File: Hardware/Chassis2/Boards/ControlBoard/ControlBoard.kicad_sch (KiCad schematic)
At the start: 16 parts, among them J1 Conn_02x08_Counter_Clockwise, J10 Conn_02x03_Counter_Clockwise, J11 TBP01R2W-508-06BE, J12 Conn_02x08_Counter_Clockwise, J13 Conn_02x03_Counter_Clockwise, J14 Conn_01x10, J2 Conn_01x02, J7 Conn_02x08_Counter_Clockwise

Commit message: update hw revision 7
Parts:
- removed J1: Conn_02x08_Counter_Clockwise, Connector_PinHeader_2.54mm:PinHeader_2x08_P2.54mm_Vertical, symbol Connector_Generic:Conn_02x08_Counter_Clockwise
- removed J14: Conn_01x10, Connector_PinHeader_2.54mm:PinHeader_1x10_P2.54mm_Vertical, symbol Connector_Generic:Conn_01x10
- removed J2: Conn_01x02, Connector_PinHeader_2.54mm:PinHeader_1x02_P2.54mm_Vertical, symbol Connector_Generic:Conn_01x02
- added J14: Conn_02x08_Counter_Clockwise, Connector_PinHeader_2.54mm:PinHeader_2x08_P2.54mm_Vertical, symbol Connector_Generic:Conn_02x08_Counter_Clockwise
- added J2: Conn_02x10_Counter_Clockwise, symbol Connector_Generic:Conn_02x10_Counter_Clockwise
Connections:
- net +12V_A: now also J2.20 (Pin_20)
- net +3.3V_A: now also J14.10 (Pin_10), J2.18 (Pin_18)
- net DRIVER_RESET: now also J2.4 (Pin_4)
- net FAULT: now also J2.2 (Pin_2)
- net GND_A: now also J14.1 (Pin_1), J14.15 (Pin_15), J14.7 (Pin_7), J2.1 (Pin_1), J2.12 (Pin_12), J2.14 (Pin_14), J2.17 (Pin_17), J2.9 (Pin_9)
- net PH_U_H: now also J2.6 (Pin_6)
- net PH_U_L: now also J2.5 (Pin_5)
- net PH_V_H: now also J2.8 (Pin_8)
- net PH_V_L: now also J2.7 (Pin_7)
- net PH_W_H: now also J2.16 (Pin_16)
- net PH_W_L: now also J2.15 (Pin_15)
- net READY: now also J2.3 (Pin_3)
- net VSENSE_DC_LINK_Y renamed VS_DC_LINK_Y
- net VSENSE_GND_Y renamed VS_GND_Y
- net VSENSE_PH_U_Y renamed VS_PH_U_Y
- net VSENSE_PH_V_Y renamed VS_PH_V_Y
- net VSENSE_PH_W_Y renamed VS_PH_W_Y
- new net +12V_IN_A: J14.16 (Pin_16)
- new net CP_BOOTSEL: J14.14 (Pin_14)
- new net CP_RESET: J14.11 (Pin_11)
- new net CP_SWCLK: J14.13 (Pin_13)
- new net CP_SWDIO: J14.12 (Pin_12)
- new net GATE_DRIVE_PWR1_ENABLE: J2.19 (Pin_19)
- new net GATE_DRIVE_PWR1_FB: J2.10 (Pin_10)
- new net GATE_DRIVE_PWR2_ENABLE: J2.13 (Pin_13)
- new net GATE_DRIVE_PWR2_FB: J2.11 (Pin_11)
- new net MP_BOOTSEL: J14.3 (Pin_3)
- new net MP_RESET: J14.6 (Pin_6)
- new net MP_SWCLK: J14.4 (Pin_4)
- new net MP_SWDIO: J14.5 (Pin_5)
- new net MP_SWO: J14.2 (Pin_2)
- new net USB_DM: J14.9 (Pin_9)
- new net USB_DP: J14.8 (Pin_8)
- no-connect marks 4 -> 2
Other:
- removed sheet USB Interface
- sheet ADC ports: added SPI_MISO_A, SPI_MOSI_A; removed SPI_RX_A, SPI_TX_A
- sheet CAN Transciever ports: added A_CAN_RX, A_CAN_TX, B_CAN_RX, B_CAN_TX; removed CAN_RX, CAN_TX
- sheet CAN Transciever1 ports: added A_CAN_RX, A_CAN_TX, B_CAN_RX, B_CAN_TX; removed CAN_RX, CAN_TX
- sheet Control ports: added CP_BOOT_SEL, CP_DEBUG_JTCK_SWCLK, CP_DEBUG_JTMS_SWDIO, CP_FDCAN2_RX, CP_FDCAN2_TX, CP_FDCAN3_RX, CP_FDCAN3_TX, CP_GATE_DRIVE_PWR2_ENABLE, CP_RESET, CP_USB_DM, CP_USB_DP, MP_BOOT_SEL, MP_CANBUS_12V_POWER_ENABLE, MP_DEBUG_JTCK_SWCLK, MP_DEBUG_JTCK_SWDIO, MP_DEBUG_NJTRST, MP_DEBUG_SWO, MP_DEBUG_TRGIO, MP_FDCAN1_RX, MP_FDCAN1_TX, MP_FDCAN2_RX, MP_FDCAN2_TX, MP_GATE_DRIVE_PWR1_ENABLE, MP_PERIPHERAL_POWER_ENABLE, MP_RESET, MP_SPI2_CS, MP_SPI2_MISO, MP_SPI2_MOSI, MP_SPI2_SCK, MP_TEMP_SENSE_2, MP_TEMP_SENSE_3, MP_USER_DIN_5, MP_USER_DIN_6, MP_USER_DIN_7, MP_USER_DIN_8, MP_USER_DOUT_1, MP_USER_DOUT_2, MP_USER_DOUT_3, MP_USER_DOUT_4, MP_VSENSE_ISO_ADC_INTERRUPT, SN_CUR_SENSE_DC_LINK_REF, SN_CUR_SENSE_DC_LINK_SIG, SN_CUR_SENSE_PH_U_REF, SN_CUR_SENSE_PH_U_SIG, SN_CUR_SENSE_PH_V_REF, SN_CUR_SENSE_PH_V_SIG, SN_CUR_SENSE_PH_W_REF, SN_CUR_SENSE_PH_W_SIG, SN_GATE_DRIVE_FAULT, SN_GATE_DRIVE_PWR1_FB, SN_GATE_DRIVE_PWR2_FB, SN_GATE_DRIVE_READY, SN_GATE_DRIVE_RESET, SN_HALL_U_ENCODER_SIN, SN_HALL_V_ENCODER_COS, SN_HALL_W, SN_MOTOR_TEMP, SN_PH_U_HIGH, SN_PH_U_LOW, SN_PH_V_HIGH, SN_PH_V_LOW, SN_PH_W_HIGH, SN_PH_W_LOW, SN_TEMP_SENSE_1, SN_THROTTLE_A, SN_THROTTLE_B, SN_USER_DIN_1, SN_USER_DIN_2, SN_USER_DIN_3, SN_USER_DIN_4; removed BOOT_SEL, CANBUS_12V_POWER_ENABLE, DC_LINK_CURRENT_SENSE, DC_LINK_CURRENT_SENSE_REF, DEBUG_JTCK-SWCLK, DEBUG_JTCK-SWDIO, DEBUG_NJTRST, DEBUG_SWO, DEBUG_TRGIO, FDCAN1_RX, FDCAN1_TX, FDCAN2_RX, FDCAN2_TX, GATE_DRIVER_FAULT, GATE_DRIVER_POWER_ENABLE, GATE_DRIVER_READY, GATE_DRIVER_RESET, HALL_U_ENCODER_SIN, HALL_V_ENCODER_COS, HALL_W, MOTOR_TEMP, NRST, PERIPHERAL_POWER_ENABLE, PHASE_U_CURRENT_SENSE, PHASE_U_CURRENT_SENSE_REF, PHASE_U_HIGH, PHASE_U_LOW, PHASE_V_CURRENT_SENSE, PHASE_V_CURRENT_SENSE_REF, PHASE_V_HIGH, PHASE_V_LOW, PHASE_W_CURRENT_SENSE, PHASE_W_CURRENT_SENSE_REF, PHASE_W_HIGH, PHASE_W_LOW, SPI1_CS, SPI2_MISO, SPI2_MOSI, SPI2_SCK, TEMP_SENSE_1, TEMP_SENSE_2, TEMP_SENSE_3, THROTTLE_A, THROTTLE_B, USART3_RX, USART3_TX, USER_DIN_1, USER_DIN_2, USER_DIN_3, USER_DIN_4, USER_DIN_5, USER_DIN_6, USER_DIN_7, USER_DIN_8, USER_DOUT_1, USER_DOUT_2, USER_DOUT_3, USER_DOUT_4, VSENSE_ISO_ADC_INTERRUPT
- note added: "Connector from gate drivers Includes multiple redundant SSO (six-switch-off) pathways: - via gate drive reset - via gate drive power enable 1 - via gate drive power enable 2 (Gate driver power enable implemnts 1oo2, with monitoring feedback)."
- note added: "Connector to IO board Digital Outputs provided here to IOBoard."
- note added: "Connector to IO board Provides dual fully isolated canbus interfaces (isolated from each-other as well) 60v tolerant"
- note added: "Control system has dual independent mcus, targeting ASIL decomposition. Independently monitored switching commands, current responses, canbus commands + faults Please see HARA under documentation for additional informaton."
- note added: "SINGLE WIRE DEBUG / PROGRAMMING USB INTERFACE TO TOP IO BOARD +12V TO CTRL BOARD FROM IO BOARD"
- note added: "This design has been implemented to provide multiple redundant pathways to SSO (Six-switch off) / STO (Safe torque-off). SSO/STO is the default safe-state of the inverter please (see Hazard And Risk Assessment documentation) Additionally, while best effort has been made to implement functional safety best practices, please note that no formal independent review has taken place, and therefore no f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"
- note added: "feedback pins are 0-3.3v binary (3.3v expected when +12v present)"
- note added: "onboard power regulator section, for 3.3v mcu power, +5v current sense, etc"
- note added: "voltage sense connector ISOLATED, HIGH VOLTAGE!"
- note removed: "Connector from gate drivers"
- note removed: "SINGLE WIRE DEBUG / PROGRAMMING"
- company: (none) -> Corzine Lab, University of California, Santa Cruz
- title: (none) -> Open Inverter Platform - Control Board
- moved on the sheet: H1, H2, H3, H4, H5, H6, H7, H8, J10, J13, J7

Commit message: Update boards
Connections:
- net GATE_DRIVE_PWR1_FB: no longer J2.10 (Pin_10)
- net GATE_DRIVE_PWR2_FB: no longer J2.11 (Pin_11)
- new net GATE_DRIVE_PWR1_FEEDBACK: J2.10 (Pin_10)
- new net GATE_DRIVE_PWR2_FEEDBACK: J2.11 (Pin_11)
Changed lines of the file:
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@@
-		)
-	)
-	(label "GATE_DRIVE_PWR2_FB"
-		(at 64.77 44.45 0)
-		(effects
-			(font
-				(size 1.27 1.27)
-			)
-			(justify left bottom)
 		)
 	)
@@
 			)
 			(justify left bottom)
-		)
-	)
-	(label "GATE_DRIVE_PWR1_FB"
-		(at 52.07 44.45 180)
-		(effects
-			(font
-				(size 1.27 1.27)
-			)
-			(justify right bottom)
 		)
 	)
@@
 		)
 	)
+	(hierarchical_label "GATE_DRIVE_PWR1_FEEDBACK"
+		(shape input)
+		(at 52.07 44.45 180)
+		(effects
+			(font
+				(size 1.27 1.27)
+			)
+			(justify right)
+		)
+	)
 	(hierarchical_label "GND_A"
 		(shape input)
@@
 		(effects
 			(font
+				(size 1.27 1.27)
+			)
+			(justify left)
+		)
+	)
+	(hierarchical_label "GATE_DRIVE_PWR2_FEEDBACK"
+		(shape input)
+		(at 64.77 44.45 0)
+		(effects
+			(font

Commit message: eod 2026-07-08
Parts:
- J11: footprint SHDR6W100P0X508_1X6_4064X850X1240P -> InverterCom:SHDR6W100P0X508_1X6_4064X850X1240P
- J2: footprint (none) -> Connector_PinSocket_2.54mm:PinSocket_2x10_P2.54mm_Vertical
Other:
- sheet TemperatureSensors ports: added MOTOR_TEMP_IN, MOTOR_TEMP_V; removed none

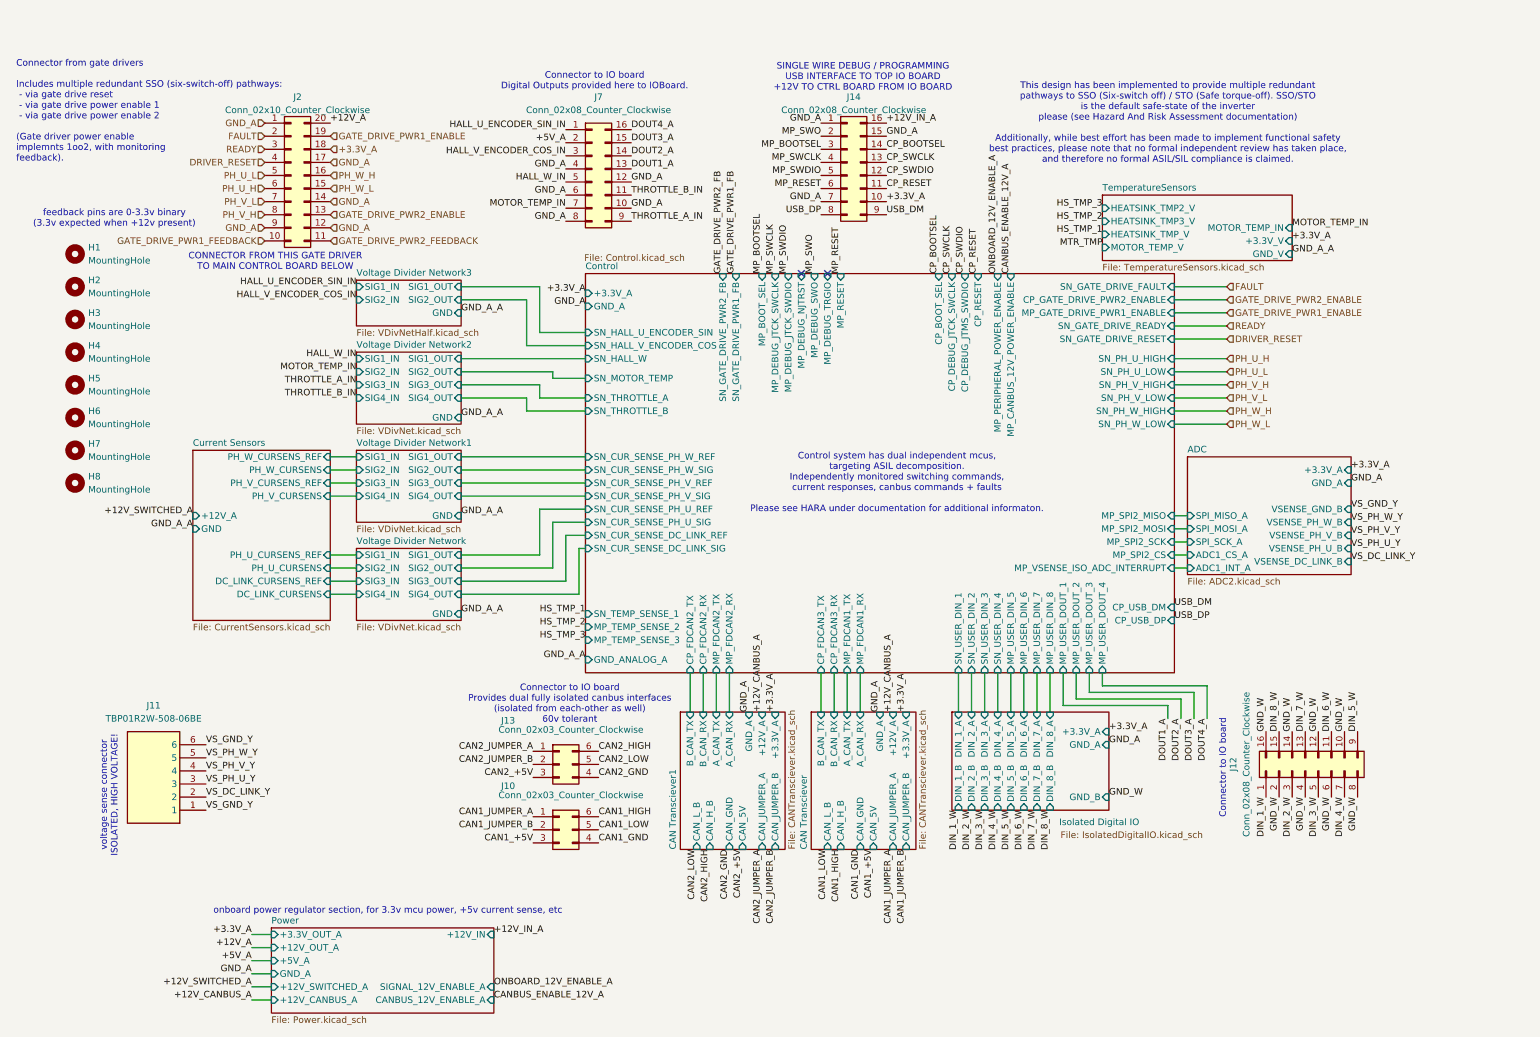
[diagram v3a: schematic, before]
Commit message: Add Schematic / Controlboard Support for Multi-Drive Mulit-Phase, DDCP
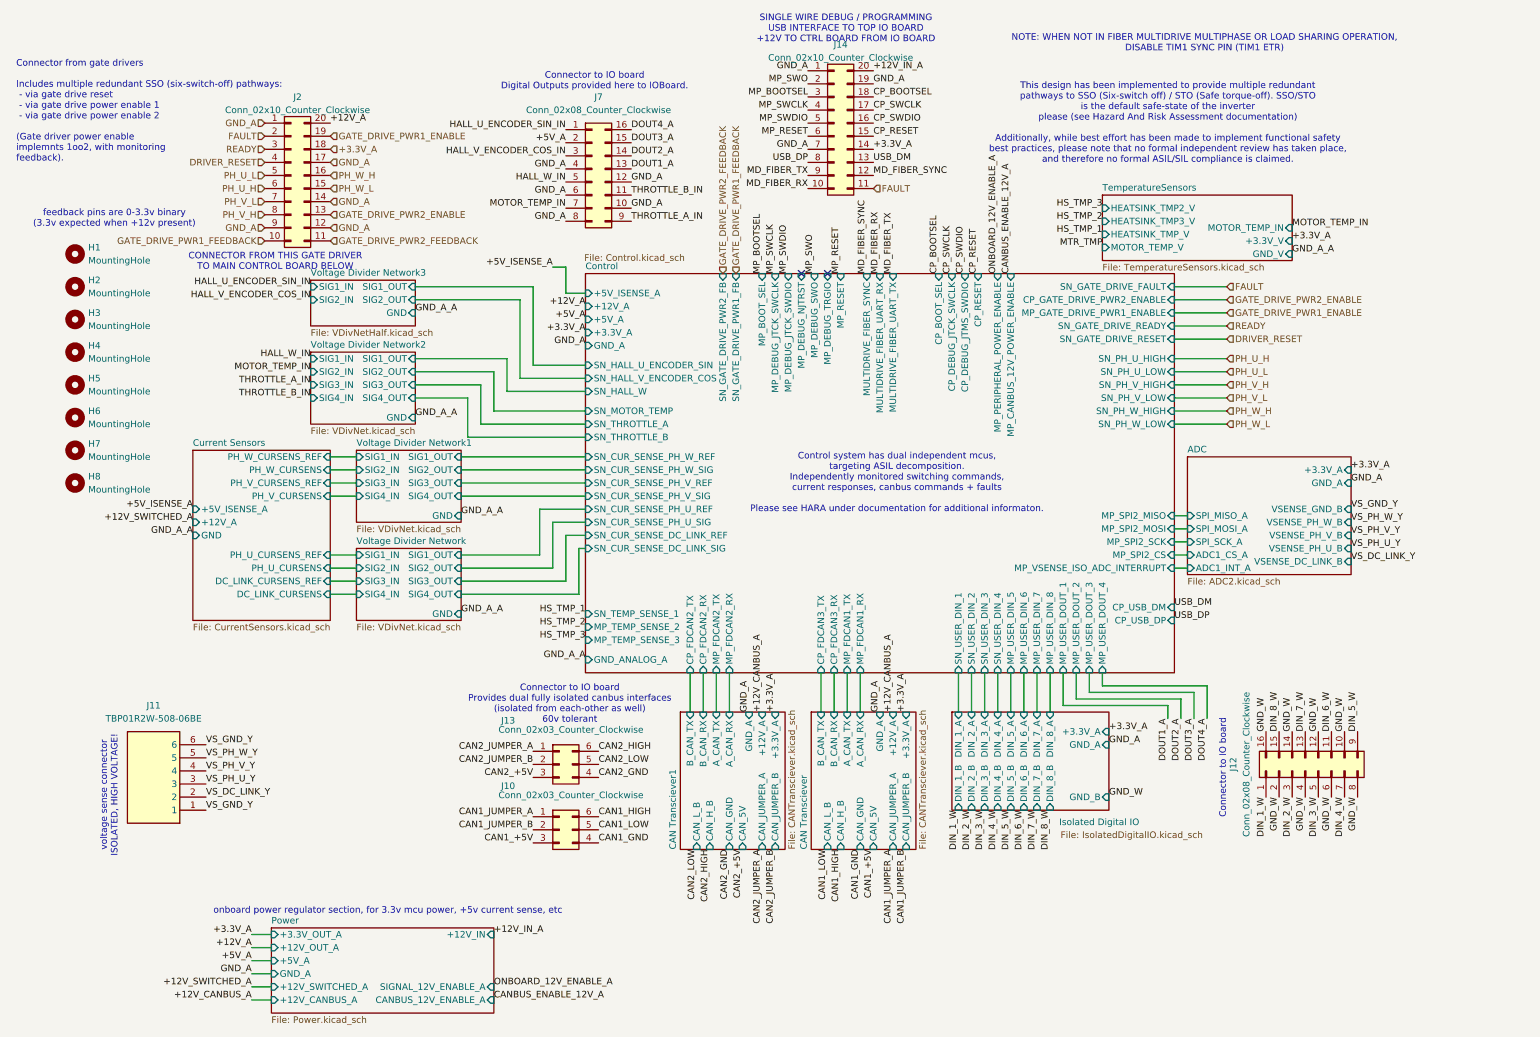
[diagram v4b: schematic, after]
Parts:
- removed J14: Conn_02x08_Counter_Clockwise, Connector_PinHeader_2.54mm:PinHeader_2x08_P2.54mm_Vertical, symbol Connector_Generic:Conn_02x08_Counter_Clockwise
- added J14: Conn_02x10_Counter_Clockwise, Connector_PinSocket_2.54mm:PinSocket_2x10_P2.54mm_Vertical, symbol Connector_Generic:Conn_02x10_Counter_Clockwise
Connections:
- net +12V_IN_A: now also J14.20 (Pin_20)
- net +3.3V_A: now also J14.14 (Pin_14)
- net CP_BOOTSEL: now also J14.18 (Pin_18)
- net CP_RESET: now also J14.15 (Pin_15)
- net CP_SWCLK: now also J14.17 (Pin_17)
- net CP_SWDIO: now also J14.16 (Pin_16)
- net FAULT: now also J14.11 (Pin_11)
- net GND_A: now also J14.1 (Pin_1), J14.19 (Pin_19), J14.7 (Pin_7)
- net MP_BOOTSEL: now also J14.3 (Pin_3)
- net MP_RESET: now also J14.6 (Pin_6)
- net MP_SWCLK: now also J14.4 (Pin_4)
- net MP_SWDIO: now also J14.5 (Pin_5)
- net MP_SWO: now also J14.2 (Pin_2)
- net USB_DM: now also J14.13 (Pin_13)
- net USB_DP: now also J14.8 (Pin_8)
- new net MD_FIBER_RX: J14.10 (Pin_10)
- new net MD_FIBER_SYNC: J14.12 (Pin_12)
- new net MD_FIBER_TX: J14.9 (Pin_9)
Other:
- sheet Control ports: added +12V_A, +5V_A, +5V_ISENSE_A, MULTIDRIVE_FIBER_SYNC, MULTIDRIVE_FIBER_UART_RX, MULTIDRIVE_FIBER_UART_TX; removed none
- sheet Current Sensors ports: added +5V_ISENSE_A; removed none
- note added: "NOTE: WHEN NOT IN FIBER MULTIDRIVE MULTIPHASE OR LOAD SHARING OPERATION, DISABLE TIM1 SYNC PIN (TIM1 ETR)"

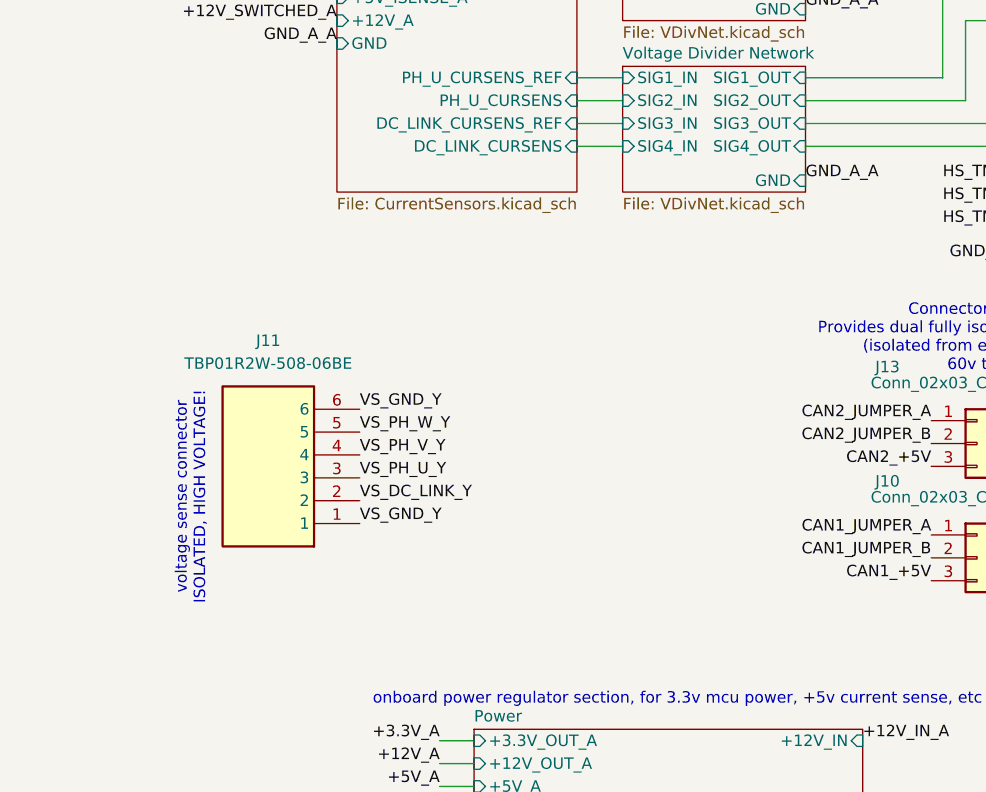
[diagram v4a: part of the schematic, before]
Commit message: Updated Gate Driver, Fixed Vsense connector on Cotnrol Board
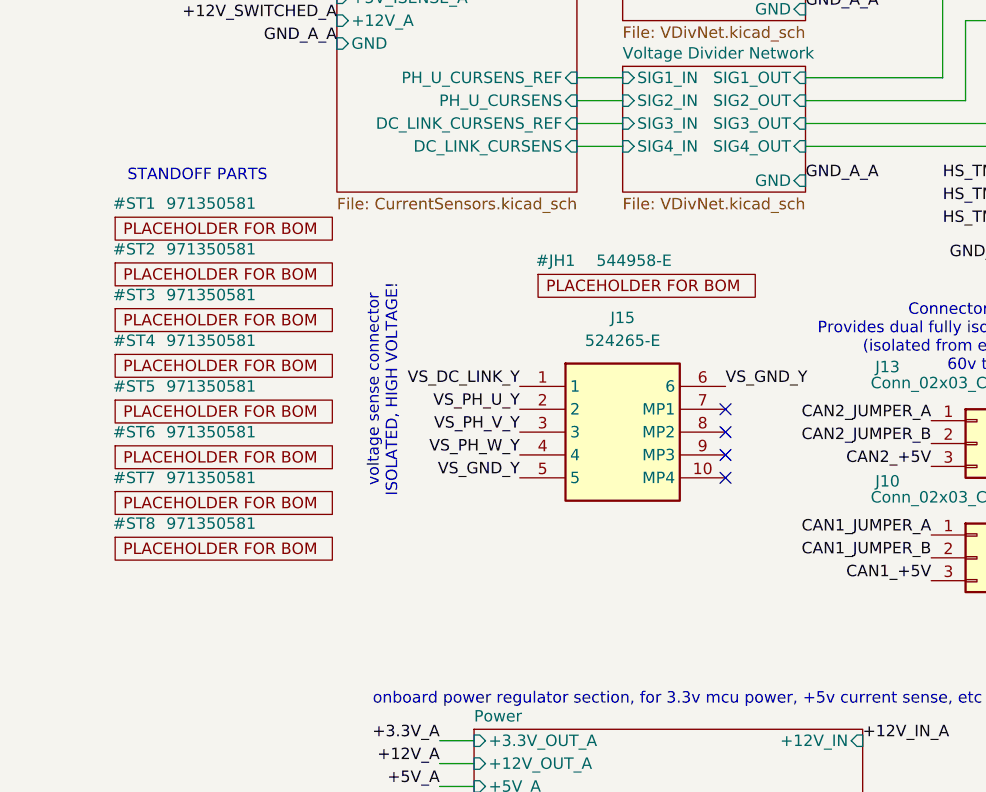
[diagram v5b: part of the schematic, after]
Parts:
- removed J11: TBP01R2W-508-06BE, InverterCom:SHDR6W100P0X508_1X6_4064X850X1240P, symbol InverterCom:TBP01R2W-508-06BE
- added J15: 524265-E, 524265E, symbol InverterCom:524265-E
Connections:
- net VS_DC_LINK_Y: now also J15.1
- net VS_GND_Y: now also J15.5, J15.6
- net VS_PH_U_Y: now also J15.2
- net VS_PH_V_Y: now also J15.3
- net VS_PH_W_Y: now also J15.4
- no-connect marks 2 -> 6
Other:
- note added: "STANDOFF PARTS"

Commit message: finalize models, parts, connectors, pn for ctrlbd
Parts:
- H1, H2, H3, H4, H5, H6, H7, H8: value MountingHole -> 971350581; footprint MountingHole:MountingHole_5.3mm_M5_ISO7380_Pad -> InverterCom:971350581; now in the parts list
- J10, J13: value Conn_02x03_Counter_Clockwise -> SSW-103-01-L-D; footprint Connector_PinHeader_2.54mm:PinHeader_2x03_P2.54mm_Vertical -> InverterCom:SSW-103-01-L-D
- J12, J7: value Conn_02x08_Counter_Clockwise -> SSW-108-01-L-D; footprint Connector_PinHeader_2.54mm:PinHeader_2x08_P2.54mm_Vertical -> InverterCom:SSW-108-01-L-D
- J14: value Conn_02x10_Counter_Clockwise -> SSW-110-01-F-D; footprint Connector_PinSocket_2.54mm:PinSocket_2x10_P2.54mm_Vertical -> InverterCom:SSW-110-01-F-D
- J15: footprint 524265E -> InverterCom:524265E
- J2: value Conn_02x10_Counter_Clockwise -> TSW-110-21-L-D-LL; footprint Connector_PinSocket_2.54mm:PinSocket_2x10_P2.54mm_Vertical -> InverterCom:PinHeader_2x10_P2.54mm_Vertical-31mm
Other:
- note removed: "STANDOFF PARTS"

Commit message: Wire harness BOMs from KiCad, board BOM re-exports, tool follows new layouts
- Four harnesses (GDVS, TSIGBT x2, CS x4, TSBCM) with per-chassis Qty
- Board BOMs move to project dirs; discovery prefers root CSV, strips
  library prefixes from footprints, reads KiCad 10 exports
- Mech list down to chassis hardware; IGBT moved to Mouser vendor
- Harness parts leave MechanicalBOM.txt (455-1135-1-ND=SXH-001T-P0.6,
  BC5011CT-ND stray cap, TSW/LA37S600/0022011042/0008500113)
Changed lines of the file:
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@@
-	)
-	(symbol
-		(lib_id "InverterCom:Placeholder")
-		(at 60.96 125.73 0)
-		(unit 1)
-		(body_style 1)
-		(exclude_from_sim no)
-		(in_bom yes)
-		(on_board yes)
-		(in_pos_files yes)
-		(dnp no)
-		(property "Reference" "#JH1"
-			(at 60.198 125.73 0)
-			(show_name no)
-			(do_not_autoplace yes)
-			(effects
-				(font
-					(size 1.27 1.27)
-				)
-				(justify left)
-			)
-		)
-		(property "Value" "544958-E"
-			(at 71.12 125.73 0)
-			(show_name no)
-			(do_not_autoplace no)
-			(effects
-				(font
-					(size 1.27 1.27)
-				)
-			)
-		)
-		(property "Footprint" ""
-			(at 60.96 125.73 0)
-			(hide yes)
-			(show_name no)
-			(do_not_autoplace no)
-			(effects
-				(font
-					(size 1.27 1.27)
-				)
-			)
-		)
-		(property "Datasheet" ""
-			(at 60.96 125.73 0)
-			(hide yes)
-			(show_name no)
-			(do_not_autoplace no)
-			(effects
-				(font
-					(size 1.27 1.27)
-				)
-			)
-		)
-		(property "Description" ""
-			(at 60.96 125.73 0)
-			(hide yes)
-			(show_name no)
-			(do_not_autoplace no)
-			(effects
-				(font
-					(size 1.27 1.27)
-				)
-			)
-		)
-		(instances
-			(project "ControlBoard"
-				(path "/66e49eb5-2741-49e2-b48a-baf482488ca8"
-					(reference "#JH1")
-					(unit 1)
-				)
-			)
-		)
 	)
 	(symbol

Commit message: Labels tool, composite board views, InverterGen5 C2 branding, even render resolution
- Labels.pdf: HV warning labels, chassis ID, per-assembly labels (label cmd)
- Board sections add composite front/back views (PCB-viewer look, mirrored
  back) and layer plots now carry the drawing sheet with true plot scale
- Branding standardized to InverterGen5 C2 (cover, footer, labels)
- STEP previews render at even resolution regardless of part aspect
- Fab part titles from info.txt PartName; ALL-CAPS handling fixed
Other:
- title: Open Inverter Platform - Control Board -> InverterGen5 - Control Board
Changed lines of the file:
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@@
 	(paper "USLetter")
 	(title_block
-		(title "Open Inverter Platform - Control Board")
+		(title "InverterGen5 - Control Board")
 		(date "2026-07-07")
 		(rev "A")
